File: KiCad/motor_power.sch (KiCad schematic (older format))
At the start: 55 parts

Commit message: Improving motor high side schematic and making it more generalized
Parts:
- removed J?: Motor connector, symbol Connector_Generic:Conn_01x18
- removed Q? (x7): Q_NMOS_DGS, symbol Device:Q_NMOS_DGS
- removed Q? (x7): Q_PMOS_DGS, symbol Device:Q_PMOS_DGS
- removed Q? (x5): Q_PMOS_SGD, symbol Device:Q_PMOS_SGD
- removed R? (x7): R, symbol Device:R
- removed R? (x19): 1K, symbol Device:R
- added Q? (x7): Q_PMOS_DGS, symbol Device:Q_PMOS_DGS
- added Q? (x7): Q_NMOS_DGS, symbol Device:Q_NMOS_DGS
- added Q? (x7): Q_PMOS_SGD, symbol Device:Q_PMOS_SGD
- added R? (x21): 1K, symbol Device:R
- added R? (x7): R, symbol Device:R
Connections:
- net labels added: col_1_motor, col_2_motor, col_3_motor, col_4_motor, col_5_motor, col_6_motor, col_7_ctrl, col_7_motor, col_8_ctrl, col_8_motor, row_a_motor, row_b_motor, row_c_motor, row_d_motor, row_e_motor, row_f_motor, row_g_motor, row_h_ctrl, row_h_motor
- net labels removed: motor_blue, motor_blue_white, motor_green_red, motor_green_white, motor_red, motor_red_white, motor_white_blue, motor_white_gray, motor_white_green, motor_white_pink, motor_white_purple, motor_white_red, motor_white_tan
- wire segments 160 -> 180
- no-connect marks 5 -> 0
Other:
- note added: "High Side\nMotor Driving"
- note added: "Low Side\nMotor\nDriving"
- moved on the sheet: Q?, R?, U?

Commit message: Switching to +5V from vcc
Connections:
- net VCC renamed +5V
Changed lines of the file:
@@
 Connection ~ 2400 7050
 $Comp
-L power:GND #PWR?
+L power:GND #PWR0121
 U 1 1 5BB27603
 P 2600 7350
-F 0 "#PWR?" H 2600 7100 50  0001 C CNN
+F 0 "#PWR0121" H 2600 7100 50  0001 C CNN
 F 1 "GND" H 2605 7177 50  0000 C CNN
 F 2 "" H 2600 7350 50  0001 C CNN
@@
 	2300 7350 2050 7350
 Connection ~ 2300 7350
-$Comp
-L power:VCC #PWR?
-U 1 1 5BB2FE84
-P 2200 7450
-F 0 "#PWR?" H 2200 7300 50  0001 C CNN
-F 1 "VCC" H 2218 7623 50  0000 C CNN
-F 2 "" H 2200 7450 50  0001 C CNN
-F 3 "" H 2200 7450 50  0001 C CNN
-	1    2200 7450
-	-1   0    0    1
-$EndComp
 Wire Wire Line
 	2200 7450 2050 7450
@@
 P 1550 800
 AR Path="/5BCCBC60" Ref="#PWR?"  Part="1"
-AR Path="/5BA75957/5BCCBC60" Ref="#PWR?"  Part="1"
-F 0 "#PWR?" H 1550 650 50  0001 C CNN
+AR Path="/5BA75957/5BCCBC60" Ref="#PWR0123"  Part="1"
+F 0 "#PWR0123" H 1550 650 50  0001 C CNN
 F 1 "+24V" H 1565 973 50  0000 C CNN
 F 2 "" H 1550 800 50  0001 C CNN
@@
 P 1950 2050
 AR Path="/5BCEAFDC" Ref="#PWR?"  Part="1"
-AR Path="/5BA75957/5BCEAFDC" Ref="#PWR?"  Part="1"
-F 0 "#PWR?" H 1950 1800 50  0001 C CNN
+AR Path="/5BA75957/5BCEAFDC" Ref="#PWR0124"  Part="1"
+F 0 "#PWR0124" H 1950 1800 50  0001 C CNN
 F 1 "GND" H 1955 1877 50  0000 C CNN
 F 2 "" H 1950 2050 50  0001 C CNN
@@
 P 3900 800
 AR Path="/5BC7E4FA" Ref="#PWR?"  Part="1"
-AR Path="/5BA75957/5BC7E4FA" Ref="#PWR?"  Part="1"
-F 0 "#PWR?" H 3900 650 50  0001 C CNN
+AR Path="/5BA75957/5BC7E4FA" Ref="#PWR0125"  Part="1"
+F 0 "#PWR0125" H 3900 650 50  0001 C CNN
 F 1 "+24V" H 3915 973 50  0000 C CNN
 F 2 "" H 3900 800 50  0001 C CNN
@@
 P 4300 2050
 AR Path="/5BC7E524" Ref="#PWR?"  Part="1"
-AR Path="/5BA75957/5BC7E524" Ref="#PWR?"  Part="1"
-F 0 "#PWR?" H 4300 1800 50  0001 C CNN
+AR Path="/5BA75957/5BC7E524" Ref="#PWR0126"  Part="1"
+F 0 "#PWR0126" H 4300 1800 50  0001 C CNN
 F 1 "GND" H 4305 1877 50  0000 C CNN
 F 2 "" H 4300 2050 50  0001 C CNN
@@
 P 6250 800
 AR Path="/5BC81D07" Ref="#PWR?"  Part="1"
-AR Path="/5BA75957/5BC81D07" Ref="#PWR?"  Part="1"
-F 0 "#PWR?" H 6250 650 50  0001 C CNN
+AR Path="/5BA75957/5BC81D07" Ref="#PWR0127"  Part="1"
+F 0 "#PWR0127" H 6250 650 50  0001 C CNN
 F 1 "+24V" H 6265 973 50  0000 C CNN
 F 2 "" H 6250 800 50  0001 C CNN
@@
 P 6650 2050
 AR Path="/5BC81D31" Ref="#PWR?"  Part="1"
-AR Path="/5BA75957/5BC81D31" Ref="#PWR?"  Part="1"
-F 0 "#PWR?" H 6650 1800 50  0001 C CNN
+AR Path="/5BA75957/5BC81D31" Ref="#PWR0128"  Part="1"
+F 0 "#PWR0128" H 6650 1800 50  0001 C CNN
 F 1 "GND" H 6655 1877 50  0000 C CNN
 F 2 "" H 6650 2050 50  0001 C CNN
@@
 P 8600 800
 AR Path="/5BC8690D" Ref="#PWR?"  Part="1"
-AR Path="/5BA75957/5BC8690D" Ref="#PWR?"  Part="1"
-F 0 "#PWR?" H 8600 650 50  0001 C CNN
+AR Path="/5BA75957/5BC8690D" Ref="#PWR0129"  Part="1"
+F 0 "#PWR0129" H 8600 650 50  0001 C CNN
 F 1 "+24V" H 8615 973 50  0000 C CNN
 F 2 "" H 8600 800 50  0001 C CNN
@@
 P 9000 2050
 AR Path="/5BC86937" Ref="#PWR?"  Part="1"
-AR Path="/5BA75957/5BC86937" Ref="#PWR?"  Part="1"
-F 0 "#PWR?" H 9000 1800 50  0001 C CNN
+AR Path="/5BA75957/5BC86937" Ref="#PWR0130"  Part="1"
+F 0 "#PWR0130" H 9000 1800 50  0001 C CNN
 F 1 "GND" H 9005 1877 50  0000 C CNN
 F 2 "" H 9000 2050 50  0001 C CNN
@@
 P 1550 2650
 AR Path="/5BC92727" Ref="#PWR?"  Part="1"
-AR Path="/5BA75957/5BC92727" Ref="#PWR?"  Part="1"
-F 0 "#PWR?" H 1550 2500 50  0001 C CNN
+AR Path="/5BA75957/5BC92727" Ref="#PWR0131"  Part="1"
+F 0 "#PWR0131" H 1550 2500 50  0001 C CNN
 F 1 "+24V" H 1565 2823 50  0000 C CNN
 F 2 "" H 1550 2650 50  0001 C CNN
@@
 P 1950 3900
 AR Path="/5BC92751" Ref="#PWR?"  Part="1"
-AR Path="/5BA75957/5BC92751" Ref="#PWR?"  Part="1"
-F 0 "#PWR?" H 1950 3650 50  0001 C CNN
+AR Path="/5BA75957/5BC92751" Ref="#PWR0132"  Part="1"
+F 0 "#PWR0132" H 1950 3650 50  0001 C CNN
 F 1 "GND" H 1955 3727 50  0000 C CNN
 F 2 "" H 1950 3900 50  0001 C CNN
@@
 P 3900 2650
 AR Path="/5BC9276C" Ref="#PWR?"  Part="1"
-AR Path="/5BA75957/5BC9276C" Ref="#PWR?"  Part="1"
-F 0 "#PWR?" H 3900 2500 50  0001 C CNN
+AR Path="/5BA75957/5BC9276C" Ref="#PWR0133"  Part="1"
+F 0 "#PWR0133" H 3900 2500 50  0001 C CNN
 F 1 "+24V" H 3915 2823 50  0000 C CNN
 F 2 "" H 3900 2650 50  0001 C CNN
@@
 P 4300 3900
 AR Path="/5BC92796" Ref="#PWR?"  Part="1"
-AR Path="/5BA75957/5BC92796" Ref="#PWR?"  Part="1"
-F 0 "#PWR?" H 4300 3650 50  0001 C CNN
+AR Path="/5BA75957/5BC92796" Ref="#PWR0134"  Part="1"
+F 0 "#PWR0134" H 4300 3650 50  0001 C CNN
 F 1 "GND" H 4305 3727 50  0000 C CNN
 F 2 "" H 4300 3900 50  0001 C CNN
@@
 P 6250 2650
 AR Path="/5BC927B1" Ref="#PWR?"  Part="1"
-AR Path="/5BA75957/5BC927B1" Ref="#PWR?"  Part="1"
-F 0 "#PWR?" H 6250 2500 50  0001 C CNN
+AR Path="/5BA75957/5BC927B1" Ref="#PWR0135"  Part="1"
+F 0 "#PWR0135" H 6250 2500 50  0001 C CNN
 F 1 "+24V" H 6265 2823 50  0000 C CNN
 F 2 "" H 6250 2650 50  0001 C CNN
@@
 P 6650 3900
 AR Path="/5BC927DB" Ref="#PWR?"  Part="1"
-AR Path="/5BA75957/5BC927DB" Ref="#PWR?"  Part="1"
-F 0 "#PWR?" H 6650 3650 50  0001 C CNN
+AR Path="/5BA75957/5BC927DB" Ref="#PWR0136"  Part="1"
+F 0 "#PWR0136" H 6650 3650 50  0001 C CNN
 F 1 "GND" H 6655 3727 50  0000 C CNN
 F 2 "" H 6650 3900 50  0001 C CNN
@@
 P 8600 2650
 AR Path="/5BC927F6" Ref="#PWR?"  Part="1"
-AR Path="/5BA75957/5BC927F6" Ref="#PWR?"  Part="1"
-F 0 "#PWR?" H 8600 2500 50  0001 C CNN
+AR Path="/5BA75957/5BC927F6" Ref="#PWR0137"  Part="1"
+F 0 "#PWR0137" H 8600 2500 50  0001 C CNN
 F 1 "+24V" H 8615 2823 50  0000 C CNN
 F 2 "" H 8600 2650 50  0001 C CNN
@@
 P 9000 3900
 AR Path="/5BC92820" Ref="#PWR?"  Part="1"
-AR Path="/5BA75957/5BC92820" Ref="#PWR?"  Part="1"
-F 0 "#PWR?" H 9000 3650 50  0001 C CNN
+AR Path="/5BA75957/5BC92820" Ref="#PWR0138"  Part="1"
+F 0 "#PWR0138" H 9000 3650 50  0001 C CNN
 F 1 "GND" H 9005 3727 50  0000 C CNN
 F 2 "" H 9000 3900 50  0001 C CNN
@@
 Text Notes 11100 5750 1    197  ~ 0
 Low Side\nMotor\nDriving
+$Comp
+L power:+5V #PWR?
+U 1 1 5BC96F7C
+P 2200 7450
+F 0 "#PWR?" H 2200 7300 50  0001 C CNN
+F 1 "+5V" H 2215 7623 50  0000 C CNN
+F 2 "" H 2200 7450 50  0001 C CNN
+F 3 "" H 2200 7450 50  0001 C CNN
+	1    2200 7450
+	-1   0    0    1
+$EndComp
 $EndSCHEMATC

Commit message: Annotating components
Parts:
- gave numbers to parts that had none: 58

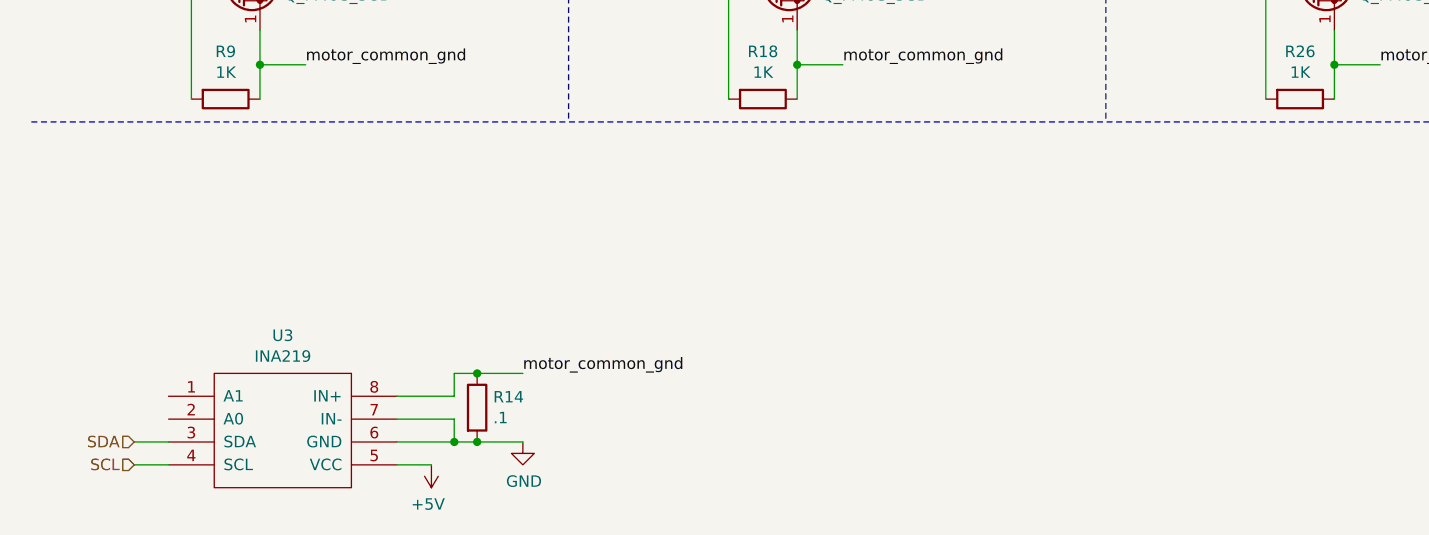
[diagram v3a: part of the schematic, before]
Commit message: Adding USB Serial page and fixing address pins in INA219
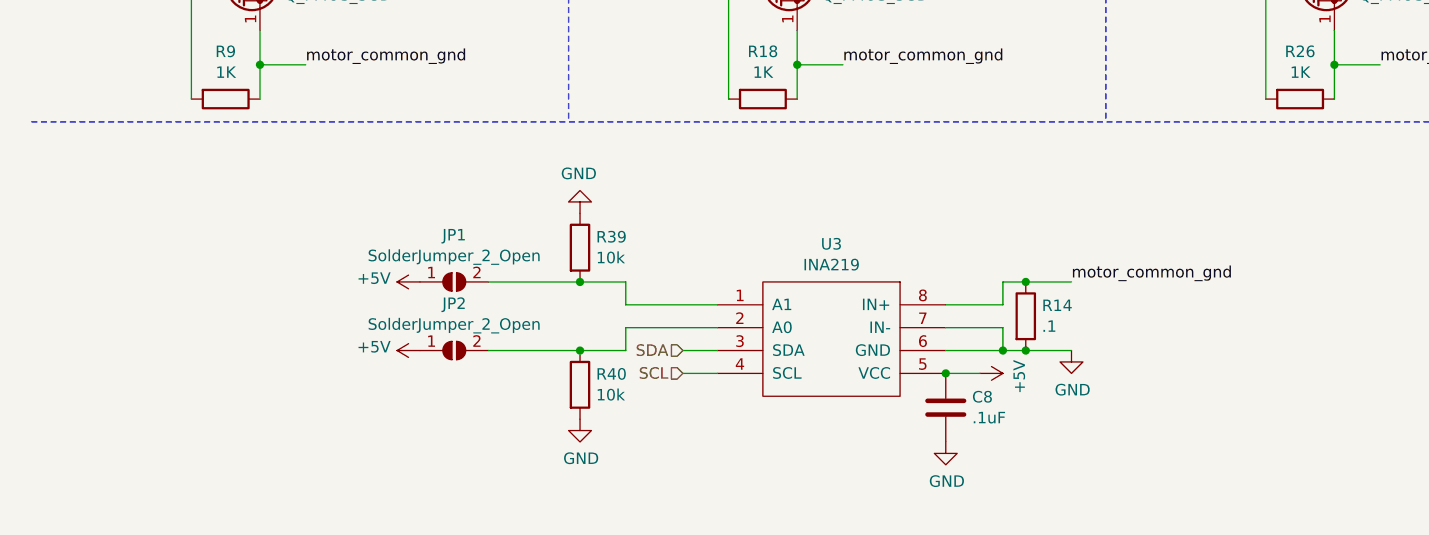
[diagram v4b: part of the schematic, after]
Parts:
- added C8: .1uF, symbol Device:C
- added JP1, JP2: SolderJumper_2_Open, symbol Jumper:SolderJumper_2_Open
- added R39, R40: 10k, symbol Device:R
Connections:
- net +5V: now also C8.1, JP1.1 (A), JP2.1 (A)
- net GND: now also C8.2, R39.1, R40.2
- net at U3.1 (A1): now also JP1.2 (B), R39.2
- net at U3.2 (A0): now also JP2.2 (B), R40.1
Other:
- moved on the sheet: R14, U3
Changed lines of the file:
@@
 $Descr A4 11693 8268
 encoding utf-8
-Sheet 2 2
+Sheet 2 3
 Title ""
 Date ""
@@
 Text Label 1650 4800 0    50   ~ 0
 motor_common_gnd
-Text Label 2600 7050 0    50   ~ 0
+Text Label 5000 6650 0    50   ~ 0
 motor_common_gnd
 $Comp
 L Device:R R14
 U 1 1 5BB1C4B9
-P 2400 7200
-F 0 "R14" H 2470 7246 50  0000 L CNN
-F 1 ".1" H 2470 7155 50  0000 L CNN
-F 2 "" V 2330 7200 50  0001 C CNN
-F 3 "~" H 2400 7200 50  0001 C CNN
-	1    2400 7200
-	1    0    0    -1
-$EndComp
-Wire Wire Line
-	2400 7350 2300 7350
-Wire Wire Line
-	2300 7350 2300 7250
-Wire Wire Line
-	2300 7250 2050 7250
-Wire Wire Line
-	2050 7150 2300 7150
-Wire Wire Line
-	2300 7150 2300 7050
-Wire Wire Line
-	2300 7050 2400 7050
-Wire Wire Line
-	2600 7050 2400 7050
-Connection ~ 2400 7050
+P 4800 6800
+F 0 "R14" H 4870 6846 50  0000 L CNN
+F 1 ".1" H 4870 6755 50  0000 L CNN
+F 2 "" V 4730 6800 50  0001 C CNN
+F 3 "~" H 4800 6800 50  0001 C CNN
+	1    4800 6800
+	1    0    0    -1
+$EndComp
+Wire Wire Line
+	4800 6950 4700 6950
+Wire Wire Line
+	4700 6950 4700 6850
+Wire Wire Line
+	4700 6850 4450 6850
+Wire Wire Line
+	4450 6750 4700 6750
+Wire Wire Line
+	4700 6750 4700 6650
+Wire Wire Line
+	4700 6650 4800 6650
+Wire Wire Line
+	5000 6650 4800 6650
+Connection ~ 4800 6650
 $Comp
 L power:GND #PWR0121
 U 1 1 5BB27603
-P 2600 7350
-F 0 "#PWR0121" H 2600 7100 50  0001 C CNN
-F 1 "GND" H 2605 7177 50  0000 C CNN
-F 2 "" H 2600 7350 50  0001 C CNN
-F 3 "" H 2600 7350 50  0001 C CNN
-	1    2600 7350
-	1    0    0    -1
-$EndComp
-Wire Wire Line
-	2600 7350 2400 7350
-Connection ~ 2400 7350
-Wire Wire Line
-	2300 7350 2050 7350
-Connection ~ 2300 7350
-Wire Wire Line
-	2200 7450 2050 7450
-Text HLabel 900  7450 0    50   Input ~ 0
+P 5000 6950
+F 0 "#PWR0121" H 5000 6700 50  0001 C CNN
+F 1 "GND" H 5005 6777 50  0000 C CNN
+F 2 "" H 5000 6950 50  0001 C CNN
+F 3 "" H 5000 6950 50  0001 C CNN
+	1    5000 6950
+	1    0    0    -1
+$EndComp
+Wire Wire Line
+	5000 6950 4800 6950
+Connection ~ 4800 6950
+Wire Wire Line
+	4700 6950 4450 6950
+Connection ~ 4700 6950
+Wire Wire Line
+	4600 7050 4450 7050
+Text HLabel 3300 7050 0    50   Input ~ 0
 SCL
 Wire Wire Line
-	900  7450 1050 7450
-Text HLabel 900  7350 0    50   Input ~ 0
+	3300 7050 3450 7050
+Text HLabel 3300 6950 0    50   Input ~ 0
 SDA
 Wire Wire Line
-	900  7350 1050 7350
+	3300 6950 3450 6950
 $Comp
 L Device:Q_PMOS_DGS Q?
@@
 L Snack_Machine:INA219 U3
 U 1 1 5BC6BBF3
-P 1550 7300
-F 0 "U3" H 1550 7715 50  0000 C CNN
-F 1 "INA219" H 1550 7624 50  0000 C CNN
-F 2 "" H 1550 7300 50  0001 C CNN
-F 3 "" H 1550 7300 50  0001 C CNN
-	1    1550 7300
+P 3950 6900
+F 0 "U3" H 3950 7315 50  0000 C CNN
+F 1 "INA219" H 3950 7224 50  0000 C CNN
+F 2 "" H 3950 6900 50  0001 C CNN
+F 3 "" H 3950 6900 50  0001 C CNN
+	1    3950 6900
 	1    0    0    -1
 $EndComp
@@
 L power:+5V #PWR0122
 U 1 1 5BC96F7C
-P 2200 7450
-F 0 "#PWR0122" H 2200 7300 50  0001 C CNN
-F 1 "+5V" H 2215 7623 50  0000 C CNN
-F 2 "" H 2200 7450 50  0001 C CNN
-F 3 "" H 2200 7450 50  0001 C CNN
-	1    2200 7450
+P 4600 7050
+F 0 "#PWR0122" H 4600 6900 50  0001 C CNN
+F 1 "+5V" H 4615 7223 50  0000 C CNN
+F 2 "" H 4600 7050 50  0001 C CNN
+F 3 "" H 4600 7050 50  0001 C CNN
+	1    4600 7050
+	0    1    1    0
+$EndComp
+$Comp
+L Jumper:SolderJumper_2_Open JP2
+U 1 1 5BC79F39
+P 2300 6950
+F 0 "JP2" H 2300 7155 50  0000 C CNN
+F 1 "SolderJumper_2_Open" H 2300 7064 50  0000 C CNN
+F 2 "" H 2300 6950 50  0001 C CNN
+F 3 "~" H 2300 6950 50  0001 C CNN
+	1    2300 6950
+	1    0    0    -1
+$EndComp
+Wire Wire Line
+	3450 6850 3050 6850
+Wire Wire Line
+	3050 6850 3050 6950
+$Comp
+L Jumper:SolderJumper_2_Open JP1
+U 1 1 5BC79CB9
+P 2300 6650
+F 0 "JP1" H 2300 6855 50  0000 C CNN
+F 1 "SolderJumper_2_Open" H 2300 6764 50  0000 C CNN
+F 2 "" H 2300 6650 50  0001 C CNN
+F 3 "~" H 2300 6650 50  0001 C CNN
+	1    2300 6650
+	1    0    0    -1
+$EndComp
+Wire Wire Line
+	3450 6750 3050 6750
+Wire Wire Line
+	3050 6750 3050 6650
+$Comp
+L Device:R R39
+U 1 1 5BCBF573
+P 2850 6500
+F 0 "R39" H 2920 6546 50  0000 L CNN
+F 1 "10k" H 2920 6455 50  0000 L CNN
+F 2 "" V 2780 6500 50  0001 C CNN
+F 3 "~" H 2850 6500 50  0001 C CNN
+	1    2850 6500
+	1    0    0    -1
+$EndComp
+$Comp
+L Device:R R40
+U 1 1 5BCBF666
+P 2850 7100
+F 0 "R40" H 2920 7146 50  0000 L CNN
+F 1 "10k" H 2920 7055 50  0000 L CNN
+F 2 "" V 2780 7100 50  0001 C CNN
+F 3 "~" H 2850 7100 50  0001 C CNN
+	1    2850 7100
+	1    0    0    -1
+$EndComp
+Connection ~ 2850 6950
+Wire Wire Line
+	2850 6950 3050 6950
+Wire Wire Line
+	2450 6650 2850 6650
+Wire Wire Line
+	2450 6950 2850 6950
+Connection ~ 2850 6650
+Wire Wire Line
+	2850 6650 3050 6650
+$Comp
+L power:GND #PWR0139
+U 1 1 5BCD264F
+P 2850 6350
+F 0 "#PWR0139" H 2850 6100 50  0001 C CNN
+F 1 "GND" H 2855 6177 50  0000 C CNN
+F 2 "" H 2850 6350 50  0001 C CNN
+F 3 "" H 2850 6350 50  0001 C CNN
+	1    2850 6350
 	-1   0    0    1
 $EndComp
+$Comp
+L power:GND #PWR0141
+U 1 1 5BCD27ED
+P 2850 7250
+F 0 "#PWR0141" H 2850 7000 50  0001 C CNN
+F 1 "GND" H 2855 7077 50  0000 C CNN
+F 2 "" H 2850 7250 50  0001 C CNN
+F 3 "" H 2850 7250 50  0001 C CNN
+	1    2850 7250
+	1    0    0    -1
+$EndComp
+$Comp
+L power:+5V #PWR0142
+U 1 1 5BCD290F
+P 2150 6650
+F 0 "#PWR0142" H 2150 6500 50  0001 C CNN
+F 1 "+5V" V 2165 6778 50  0000 L CNN
+F 2 "" H 2150 6650 50  0001 C CNN
+F 3 "" H 2150 6650 50  0001 C CNN
+	1    2150 6650
+	0    -1   -1   0
+$EndComp
+$Comp
+L power:+5V #PWR0143
+U 1 1 5BCD2A57
+P 2150 6950
+F 0 "#PWR0143" H 2150 6800 50  0001 C CNN
+F 1 "+5V" V 2165 7078 50  0000 L CNN
+F 2 "" H 2150 6950 50  0001 C CNN
+F 3 "" H 2150 6950 50  0001 C CNN
+	1    2150 6950
+	0    -1   -1   0
+$EndComp
+$Comp
+L Device:C C8
+U 1 1 5BCD303F
+P 4450 7200
+F 0 "C8" H 4565 7246 50  0000 L CNN
+F 1 ".1uF" H 4565 7155 50  0000 L CNN
+F 2 "" H 4488 7050 50  0001 C CNN
+F 3 "~" H 4450 7200 50  0001 C CNN
+	1    4450 7200
+	1    0    0    -1
+$EndComp
+Connection ~ 4450 7050
+$Comp
+L power:GND #PWR0144
+U 1 1 5BCEEBDE
+P 4450 7350
+F 0 "#PWR0144" H 4450 7100 50  0001 C CNN
+F 1 "GND" H 4455 7177 50  0000 C CNN
+F 2 "" H 4450 7350 50  0001 C CNN
+F 3 "" H 4450 7350 50  0001 C CNN
+	1    4450 7350
+	1    0    0    -1
+$EndComp
 $EndSCHEMATC
